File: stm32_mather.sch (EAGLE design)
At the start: 50 parts

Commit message: ledとか追加した
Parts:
- added LED2: (no value), user_leds:1608LED
- added R14, R15: 10k, user_rcl:R_REG
- added R_I1: (no value), user_rcl:R_SHUGOU
- added U$15: RGB_LED, user_leds:RGB_LED
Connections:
- new net B_LED: MCU1.35, R_I1.6
- new net ERROR: MCU1.33_PB12<, R_I1.8
- new net G_LED: MCU1.34, R_I1.7
- new net N$10: R_I1.1, U$15.R_K
- new net N$29: R_I1.2, U$15.G_K
- new net N$31: R_I1.3, U$15.B_K
- new net N$32: LED2.A, R_I1.4
- net GND: now also LED2.K, U$15.B_A, U$15.G_A, U$15.R_A
- net USART1_RX: now also R14.1
- net USART1_TX: now also R15.1
- net V3.3: now also R14.2, R15.2, R_I1.5
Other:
- moved on the sheet: C13, C14, R10, R4, R5, R9

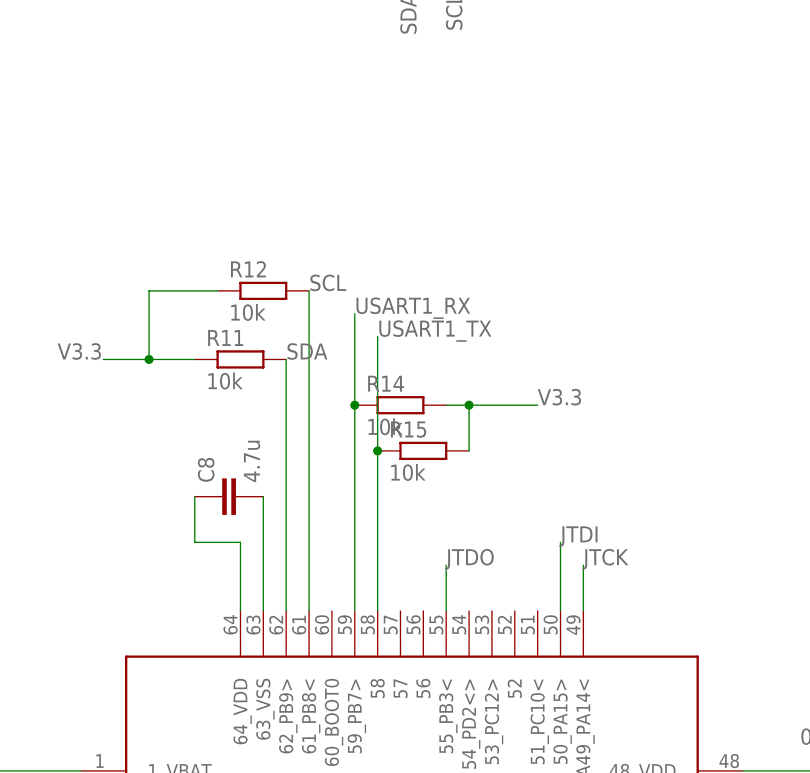
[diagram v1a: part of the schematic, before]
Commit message: bootピンの設定をした
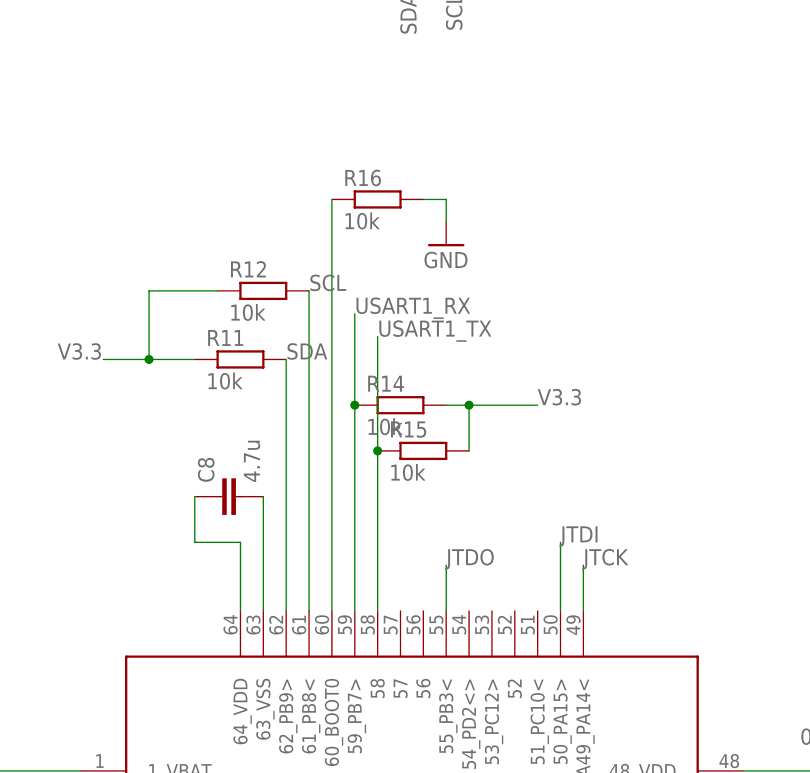
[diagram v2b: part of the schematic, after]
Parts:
- added R16: 10k, user_rcl:R_REG
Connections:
- new net N$33: MCU1.60_BOOT0, R16.1
- net GND: now also R16.2
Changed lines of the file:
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@@
 <part name="LED2" library="user_leds" deviceset="1608LED" device=""/>
 <part name="GND17" library="supply1" library_urn="urn:adsk.eagle:library:371" deviceset="GND" device=""/>
+<part name="R16" library="user_rcl" deviceset="R_REG" device="" value="10k"/>
+<part name="GND18" library="supply1" library_urn="urn:adsk.eagle:library:371" deviceset="GND" device=""/>
 </parts>
 <sheets>
@@
 <instance part="GND17" gate="1" x="190.5" y="93.98" smashed="yes">
 <attribute name="VALUE" x="187.96" y="91.44" size="1.778" layer="96"/>
+</instance>
+<instance part="R16" gate="G$1" x="101.6" y="165.1" smashed="yes">
+<attribute name="NAME" x="97.79" y="166.5986" size="1.778" layer="95"/>
+<attribute name="VALUE" x="97.79" y="161.798" size="1.778" layer="96"/>
+</instance>
+<instance part="GND18" gate="1" x="109.22" y="160.02" smashed="yes">
+<attribute name="VALUE" x="106.68" y="157.48" size="1.778" layer="96"/>
 </instance>
 </instances>
@@
 <junction x="200.66" y="99.06"/>
 </segment>
+<segment>
+<pinref part="R16" gate="G$1" pin="2"/>
+<wire x1="106.68" y1="165.1" x2="109.22" y2="165.1" width="0.1524" layer="91"/>
+<pinref part="GND18" gate="1" pin="GND"/>
+<wire x1="109.22" y1="165.1" x2="109.22" y2="162.56" width="0.1524" layer="91"/>
+</segment>
 </net>
 <net name="V3.3" class="0">
@@
 </segment>
 </net>
+<net name="N$33" class="0">
+<segment>
+<pinref part="R16" gate="G$1" pin="1"/>
+<pinref part="MCU1" gate="G$1" pin="60_BOOT0"/>
+<wire x1="96.52" y1="165.1" x2="96.52" y2="119.38" width="0.1524" layer="91"/>
+</segment>
+</net>
